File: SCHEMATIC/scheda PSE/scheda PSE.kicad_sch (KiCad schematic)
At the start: 49 parts

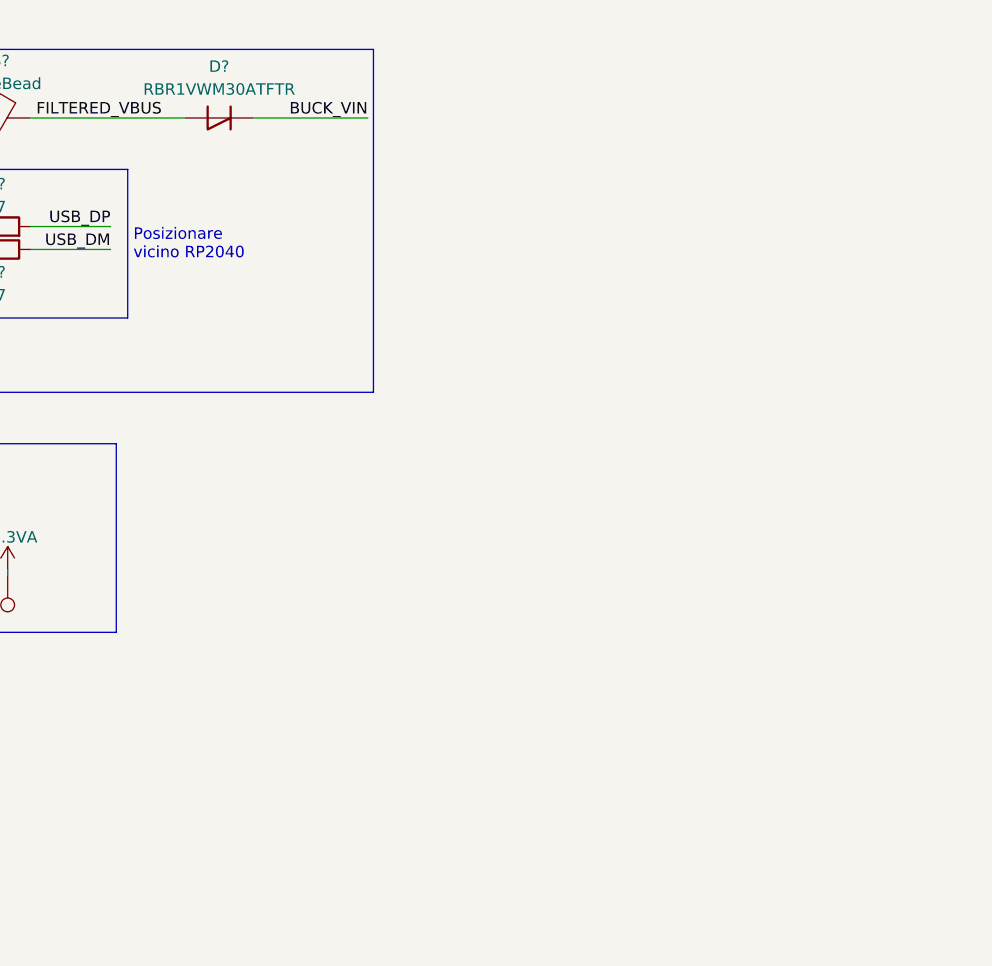
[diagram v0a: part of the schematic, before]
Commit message: aggiunto GPS, LED_alive, Buzzer, RGB_WS2812B
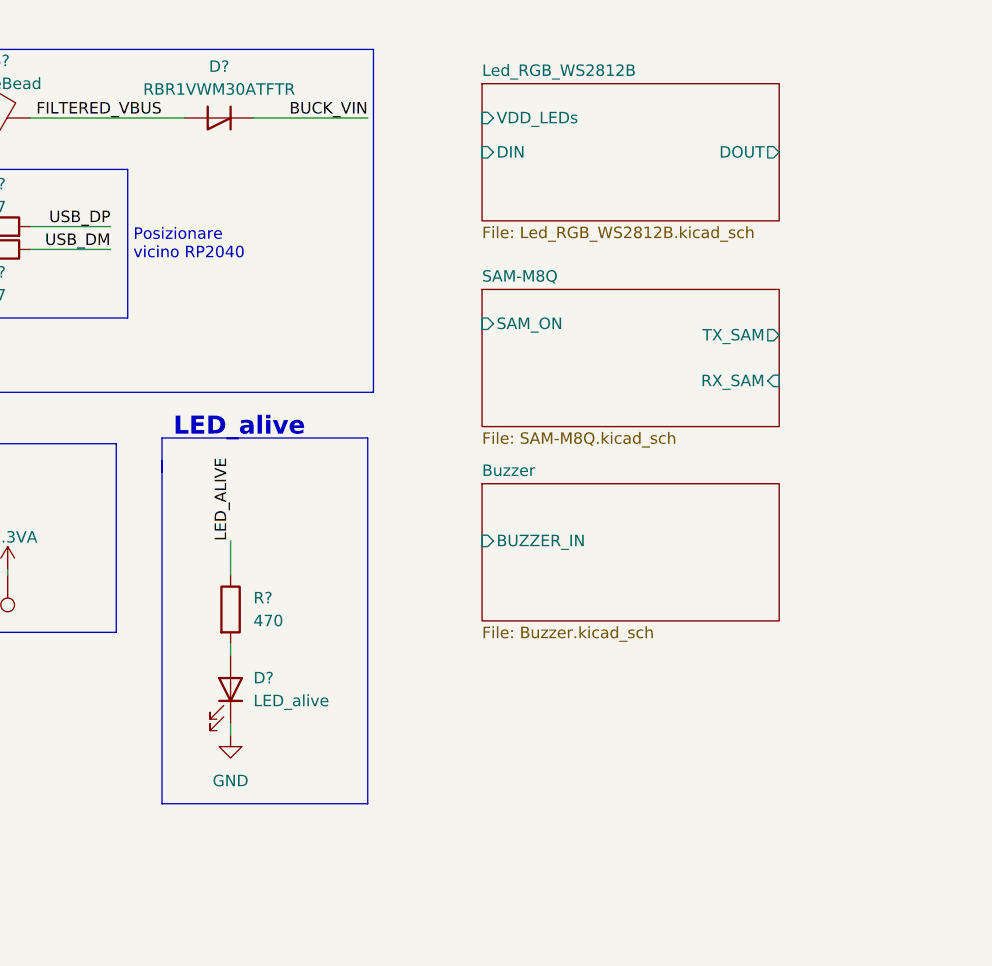
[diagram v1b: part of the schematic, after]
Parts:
- added D?: LED_alive, symbol Device:LED
- added R?: 470, symbol Device:R
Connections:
- net GND: now also D?.1 (K)
- new net: D?.2 (A), R?.2
- new net LED_ALIVE: R?.1
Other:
- added sheet Buzzer (Buzzer.kicad_sch)
- added sheet Led_RGB_WS2812B (Led_RGB_WS2812B.kicad_sch)
- added sheet SAM-M8Q (SAM-M8Q.kicad_sch)
- note added: "LED_alive"

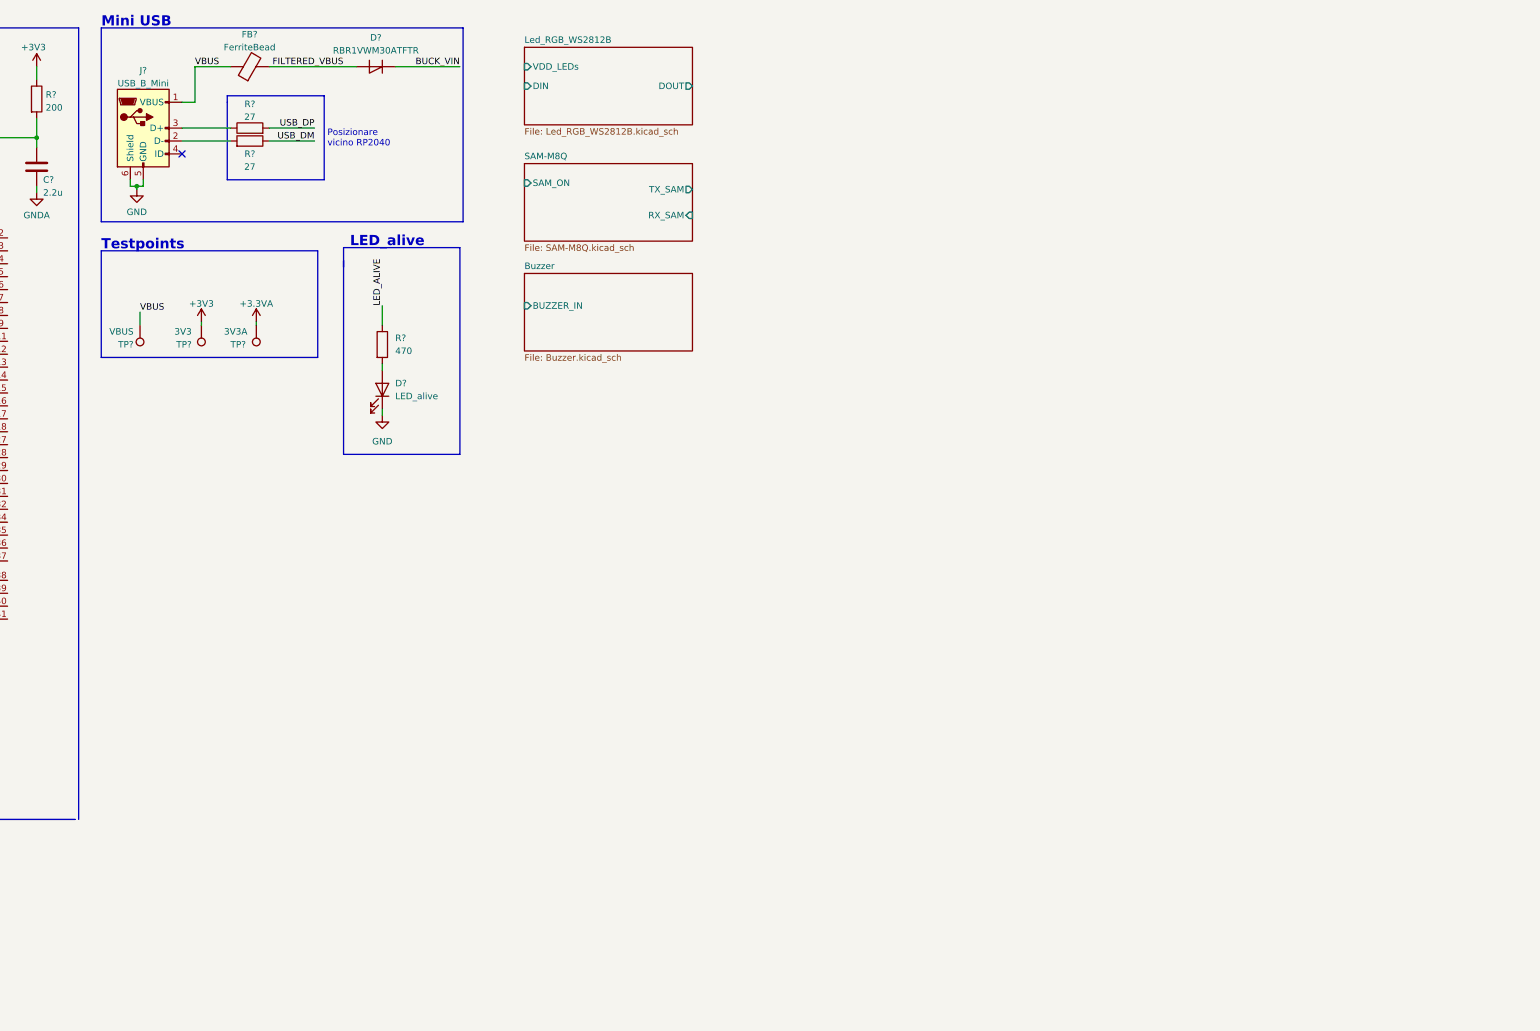
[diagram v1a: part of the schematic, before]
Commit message: Add files via upload
aggiunto display, accelerometro, sensore temp
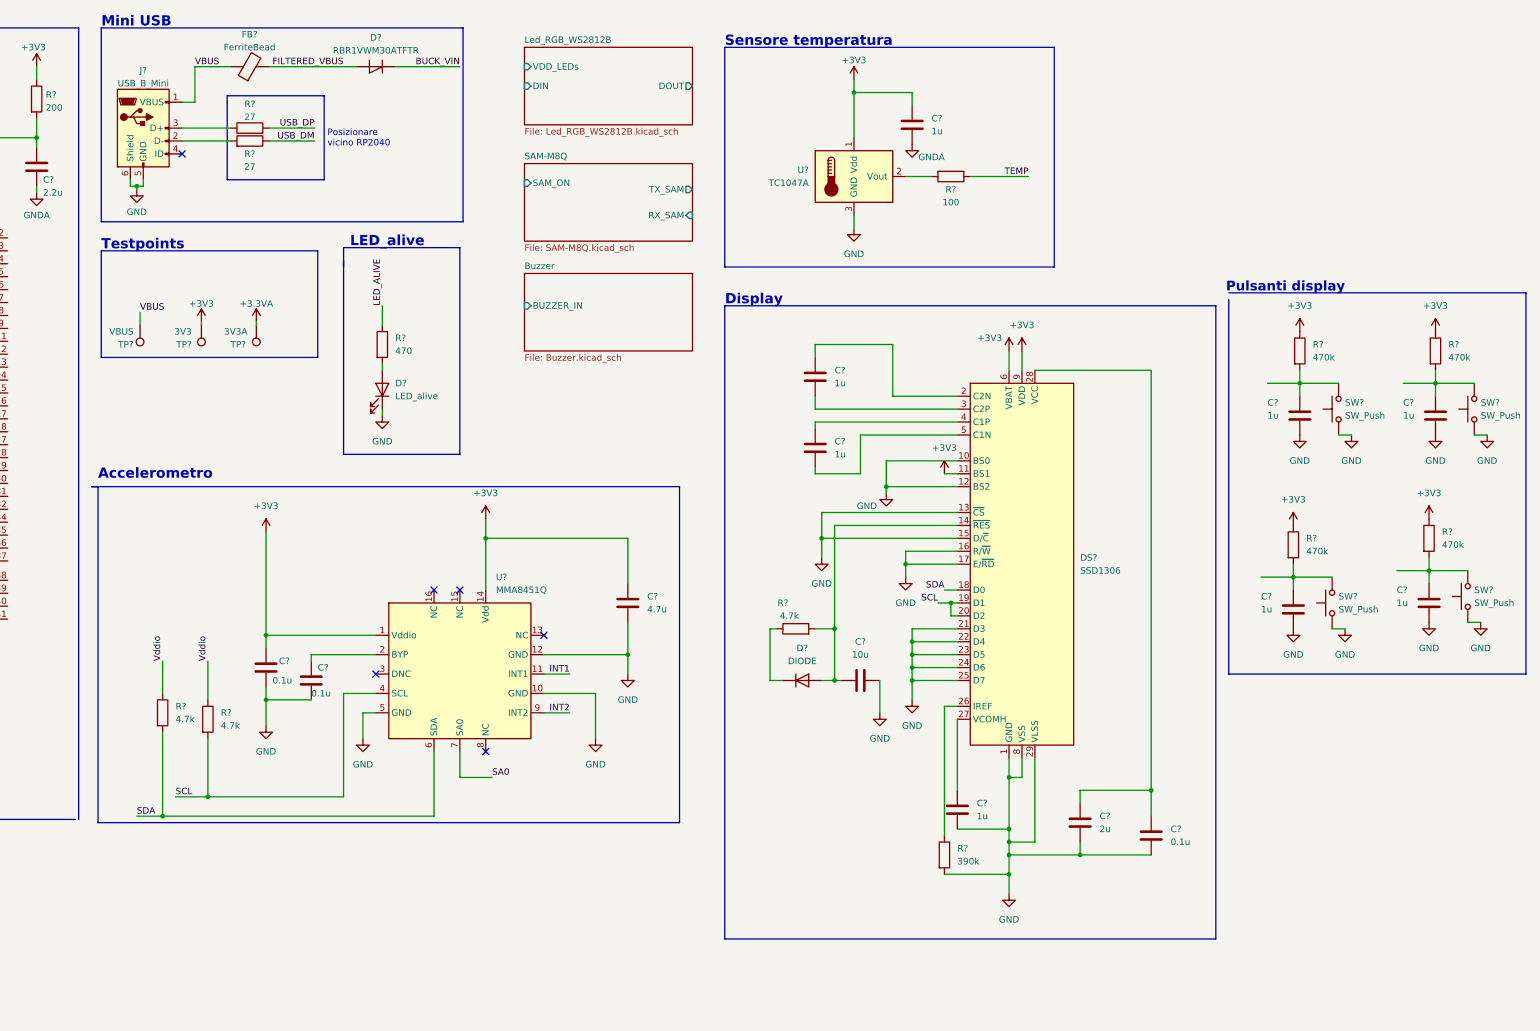
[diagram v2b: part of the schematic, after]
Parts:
- added C? (x8): 1u, symbol Device:C
- added C? (x3): 0.1u, symbol Device:C
- added C?: 10u, symbol Device:C
- added C?: 4.7u, symbol Device:C
- added C?: 2u, symbol Device:C
- added D?: DIODE, symbol Simulation_SPICE:DIODE
- added DS?: SSD1306, Display:OLED-128O064D, symbol Display_Graphic:OLED-128O064D
- added R? (x4): 470k, symbol Device:R
- added R? (x3): 4.7k, symbol Device:R
- added R?: 390k, symbol Device:R
- added R?: 100, symbol Device:R
- added SW? (x4): SW_Push, symbol Switch:SW_Push
- added U?: TC1047A, Package_TO_SOT_SMD:SOT-23, symbol Sensor_Temperature:TC1047AxNB
- added U?: MMA8451Q, symbol MMA8451Q:MMA8451Q
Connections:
- net +3V3: now also C?.1, C?.1, C?.1, DS?.11 (BS1), DS?.6 (VBAT), DS?.9 (VDD), R?.1, R?.1, R?.1, R?.1, U?.1 (Vdd), U?.1 (Vddio), U?.14 (Vdd)
- net GND: now also C?.2, C?.2, C?.2, C?.2, C?.2, C?.2, C?.2, C?.2, C?.2, C?.2, C?.2, DS?.1 (GND), DS?.10 (BS0), DS?.12 (BS2), DS?.13 (~{CS}), DS?.15 (D/~{C}), DS?.16 (R/~{W}), DS?.17 (E/~{RD}), DS?.21 (D3), DS?.22 (D4), DS?.23 (D5), DS?.24 (D6), DS?.25 (D7), DS?.29 (VLSS), DS?.30 (GND), DS?.8 (VSS), R?.2, SW?.1, SW?.1, SW?.1, SW?.1, U?.10 (GND), U?.12 (GND), U?.3 (GND), U?.5 (GND)
- net GNDA: now also C?.2
- new net: R?.2, U?.2 (Vout)
- new net: C?.1, R?.2, SW?.2 (x4)
- new net: C?.1, C?.1, DS?.28 (VCC)
- new net: C?.1, DS?.4 (C1P)
- new net: C?.2, DS?.5 (C1N)
- new net: C?.1, U?.2 (BYP)
- new net: C?.1, D?.1 (A), DS?.14 (~{RES}), R?.2
- new net: D?.2 (K), R?.1
- new net: DS?.26 (IREF), R?.1
- new net: C?.1, DS?.27 (VCOMH)
- new net: C?.1, DS?.2 (C2N)
- new net: C?.2, DS?.3 (C2P)
- new net INT1: U?.11 (INT1)
- new net INT2: U?.9 (INT2)
- new net SA0: U?.7 (SA0)
- new net SCL: DS?.19 (D1), DS?.20 (D2), R?.2, U?.4 (SCL)
- new net SDA: DS?.18 (D0), R?.2, U?.6 (SDA)
- new net TEMP: R?.1
- new net Vddio: R?.1, R?.1
- no-connect marks 1 -> 6
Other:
- note added: "Accelerometro"
- note added: "Display"
- note added: "Pulsanti display"
- note added: "Sensore temperatura"

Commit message: Sistemato tutto lo schematico con fogli gerarchici
Sistemato lo schematico, ordinato tutti i componenti nei vari fogli gerarchici.
aggiunto ldo e sistemato il buck converter. aggiunti anche i terminali a vite per le connessioni esterne
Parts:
- removed C? (x12): 100n, symbol Device:C
- removed C? (x8): 1u, symbol Device:C
- removed C? (x3): 0.1u, symbol Device:C
- removed C? (x3): 2.2u, symbol Device:C
- removed C? (x3): 10u, symbol Device:C
- removed C? (x2): 18p, symbol Device:C
- removed C? (x2): 22u, symbol Device:C
- removed C?: 4.7u, symbol Device:C
- removed C?: 2u, symbol Device:C
- removed C?: DNP 100n, symbol Device:C
- removed C?: 100n, symbol Device:C_Small
- removed D?: 3V3_LED, symbol Device:LED
- removed D?: RBR1VWM30ATFTR, symbol Device:D_Shockley
- removed D?: DIODE, symbol Simulation_SPICE:DIODE
- removed D?: LED_alive, symbol Device:LED
- removed DS?: SSD1306, Display:OLED-128O064D, symbol Display_Graphic:OLED-128O064D
- removed FB?: FerriteBead, symbol Device:FerriteBead
- removed J?: Debug, symbol Connector_Generic:Conn_02x03_Counter_Clockwise
- removed J?: USB_B_Mini, symbol Connector:USB_B_Mini
- removed L?: 2.2u, symbol Device:L
- removed R? (x4): 470k, symbol Device:R
- removed R? (x2): 1k, symbol Device:R
- removed R? (x3): 4.7k, symbol Device:R
- removed R? (x2): 27, symbol Device:R
- removed R?: 510, symbol Device:R
- removed R?: 10K, symbol Device:R
- removed R?: 470, symbol Device:R
- removed R?: 33k, symbol Device:R
- removed R?: 390k, symbol Device:R
- removed R?: 200, symbol Device:R
- removed R? (x3): 10k, symbol Device:R
- removed R?: 100, symbol Device:R
- removed SW?: RESET_SW, symbol Switch:SW_Push
- removed SW? (x4): SW_Push, symbol Switch:SW_Push
- removed SW?: PROG_SW, symbol Switch:SW_Push
- removed TP?: VBUS, symbol Connector:TestPoint
- removed TP?: 3V3, symbol Connector:TestPoint
- removed TP?: 3V3A, symbol Connector:TestPoint
- removed U?: TC1047A, Package_TO_SOT_SMD:SOT-23, symbol Sensor_Temperature:TC1047AxNB
- removed U?: W25Q16JVUSSQ, _MIA footprint:SOIC8-150mils, symbol _PSE 2022:W25Q16JVUSSQ
- removed U?: MMA8451Q, symbol MMA8451Q:MMA8451Q
- removed U?: TPS563201, Package_TO_SOT_SMD:SOT-23-6, symbol Regulator_Switching:TPS563200
- removed U?: RP2040, _PSE:QFN40P700X700X90-57N-D, symbol _PSE 2022:RP2040
- removed Y?: 12MHz, symbol Device:Crystal_GND23
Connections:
- no-connect marks 6 -> 0
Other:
- removed sheet Buzzer
- removed sheet SAM-M8Q
- added sheet Alimentazione (alimentazione.kicad_sch)
- added sheet Interfaccia utente (Interfaccia_utente.kicad_sch)
- added sheet RP2040 (rp2040.kicad_sch)
- added sheet Sensori (sensori.kicad_sch)
- sheet Led_RGB_WS2812B ports: added none; removed DOUT
- note removed: "Accelerometro"
- note removed: "Buck converter: Vin 4.5-17V, Vout 3.3V 3A (max)"
- note removed: "Circuito principale RP2040"
- note removed: "Crystal"
- note removed: "Debug"
- note removed: "Display"
- note removed: "Flash"
- note removed: "LED_alive"
- note removed: "Mini USB"
- note removed: "NOTA: posizionare vicino i pin: IOVDD, USB_VDD"
- note removed: "Posizionare vicino RP2040"
- note removed: "Pulsanti display"
- note removed: "Sensore temperatura"
- note removed: "Testpoints"
- note removed: "VOUT = 0.765*(1+(R?/R?))"
